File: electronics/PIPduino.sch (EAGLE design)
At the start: 45 parts, among them IC1 ATmega328P\, J1 ISP|SPI, U1 NCP5500, X1 16MHz

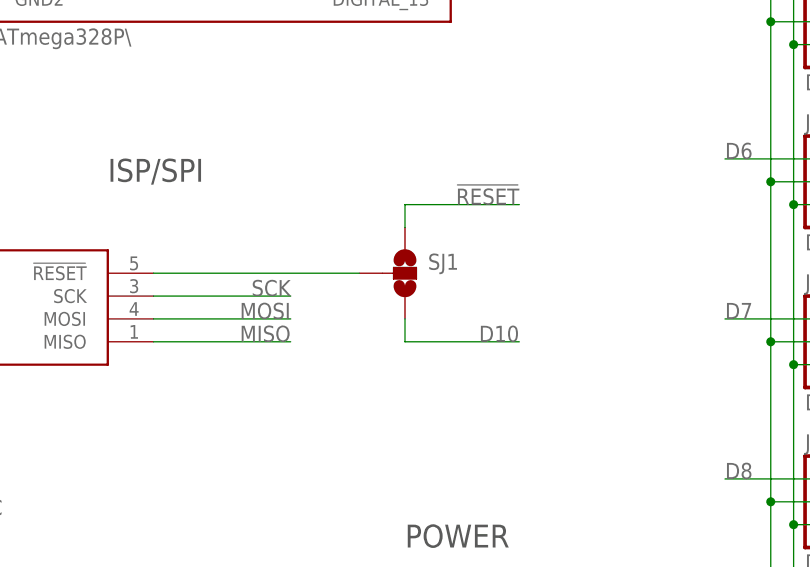
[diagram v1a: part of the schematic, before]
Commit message: Updated 3-way jumper selector
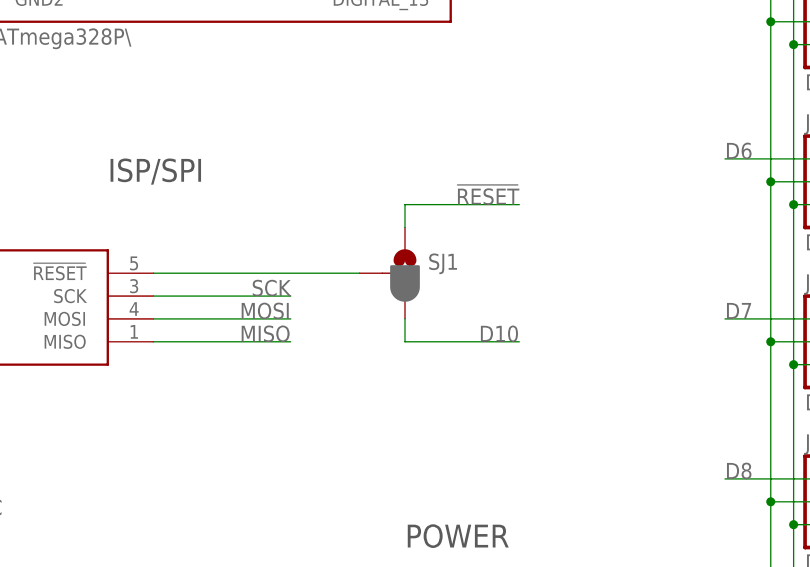
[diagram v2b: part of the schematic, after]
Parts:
- SJ1: value (none) -> JUMPER-PAD-3-2OF3_NC_BY_PASTE; device SparkFun-Passives:SOLDERJUMPER_2WAYS -> SparkFun-Passives:JUMPER-PAD-3-2OF3_NC_BY_PASTE
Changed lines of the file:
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@@
 <part name="U$9" library="SparkFun" deviceset="5V" device="" value="VCC"/>
 <part name="C5" library="rcl" deviceset="C-US" device="C1206" value="106"/>
-<part name="SJ1" library="SparkFun-Passives" deviceset="SOLDERJUMPER_2WAY" device="S"/>
+<part name="SJ1" library="SparkFun-Passives" deviceset="JUMPER-PAD-3-2OF3_NC_BY_PASTE" device="" value=""/>
 <part name="R3" library="rcl" deviceset="R-US_" device="R0603" value="330"/>
 <part name="D13" library="bt_opto" deviceset="LED" device="3MM"/>
